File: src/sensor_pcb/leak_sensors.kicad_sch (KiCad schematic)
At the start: 0 parts

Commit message: added connectors
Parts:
- added D1: APHHS1005LSECK/J3-PF, LED_SMD:LED_0402_1005Metric, symbol #dzdb:s_dio/D-KIN-APHHS1005LSECK/J3-PF
- added Q1: NPN BJT 40V 200mA, Package_TO_SOT_SMD:SOT-23, symbol #dzdb:s_misc/Q-NPN-200-SOT23
- added R1, R3: 1k, Resistor_SMD:R_0603_1608Metric, symbol #dzdb:g_res/R-1k-0603
- added R2: 240, Resistor_SMD:R_0603_1608Metric, symbol #dzdb:g_res/R-240-0603
- added R4: 27k, Resistor_SMD:R_0603_1608Metric, symbol #dzdb:g_res/R-27k-0603
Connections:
- new net: D1.2 (A), R2.2
- new net: Q1.1 (B), R3.2, R4.2
- new net GND: D1.1 (K), R1.2
- new net Probe: R3.1
- new net VCC: Q1.2 (E), R4.1
- new net signal: Q1.3 (C), R1.1, R2.1
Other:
- note added: "currently high voltage -> leak detected, could use jumper to change that"
- note added: "will probably want to have multiple ones"

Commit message: 8 pin connectors added
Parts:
- removed D1: APHHS1005LSECK/J3-PF, LED_SMD:LED_0402_1005Metric, symbol #dzdb:s_dio/D-KIN-APHHS1005LSECK/J3-PF
- removed Q1: NPN BJT 40V 200mA, Package_TO_SOT_SMD:SOT-23, symbol #dzdb:s_misc/Q-NPN-200-SOT23
- removed R1, R3: 1k, Resistor_SMD:R_0603_1608Metric, symbol #dzdb:g_res/R-1k-0603
- removed R2: 240, Resistor_SMD:R_0603_1608Metric, symbol #dzdb:g_res/R-240-0603
- removed R4: 27k, Resistor_SMD:R_0603_1608Metric, symbol #dzdb:g_res/R-27k-0603
- added D2, D3: APHHS1005LSECK/J3-PF, LED_SMD:LED_0402_1005Metric, symbol #dzdb:s_dio/D-KIN-APHHS1005LSECK/J3-PF
- added Q2, Q3: NPN BJT 40V 200mA, Package_TO_SOT_SMD:SOT-23, symbol #dzdb:s_misc/Q-NPN-200-SOT23
- added R12, R16: 27k, Resistor_SMD:R_0603_1608Metric, symbol #dzdb:g_res/R-27k-0603
- added R13, R15, R17, R9: 1k, Resistor_SMD:R_0603_1608Metric, symbol #dzdb:g_res/R-1k-0603
- added R14, R18: 240, Resistor_SMD:R_0603_1608Metric, symbol #dzdb:g_res/R-240-0603
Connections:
- net GND: now also D2.1 (K), D3.1 (K), R13.2, R17.2
- net VCC: now also Q2.2 (E), Q3.2 (E), R12.1, R16.1
- new net: Q3.1 (B), R15.2, R16.2
- new net: D2.2 (A), R14.2
- new net: Q2.1 (B), R12.2, R9.2
- new net: D3.2 (A), R18.2
- new net Probe 1.1: R9.1
- new net Probe 2.1: R15.1
- new net sig 1.1: Q2.3 (C), R13.1, R14.1
- new net sig 2.1: Q3.3 (C), R17.1, R18.1
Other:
- note removed: "currently high voltage -> leak detected, could use jumper to change that"
- note removed: "will probably want to have multiple ones"

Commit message: v1 complete
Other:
- company: (none) -> Giacomo Raggi
- title: (none) -> Sensor_pcb: leak sensors
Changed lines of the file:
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@@
 	(generator_version "9.0")
 	(paper "A4")
+	(title_block
+		(title "Sensor_pcb: leak sensors")
+		(date "2025-10-21")
+		(company "Giacomo Raggi")
+	)
 	(rectangle
 		(start 27.94 31.75)

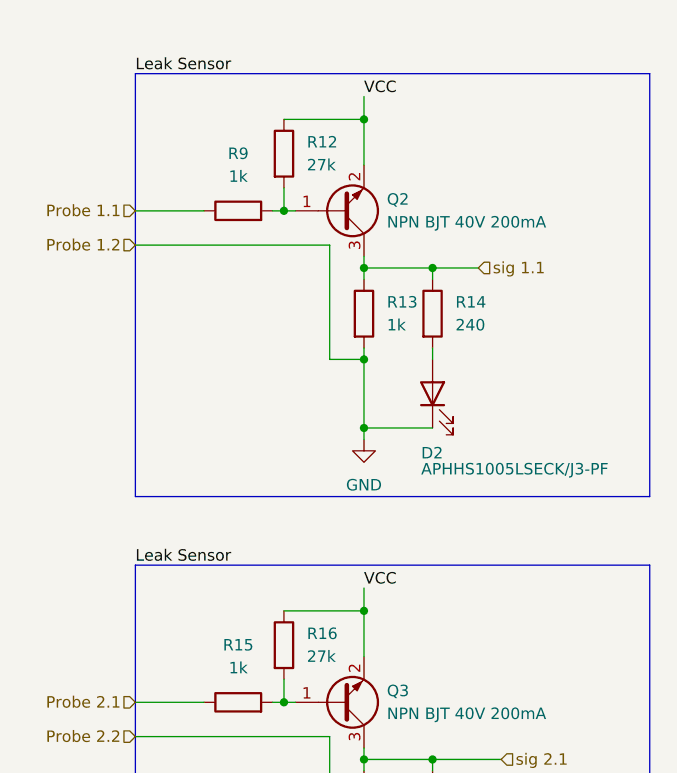
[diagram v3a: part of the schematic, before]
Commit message: schematic update
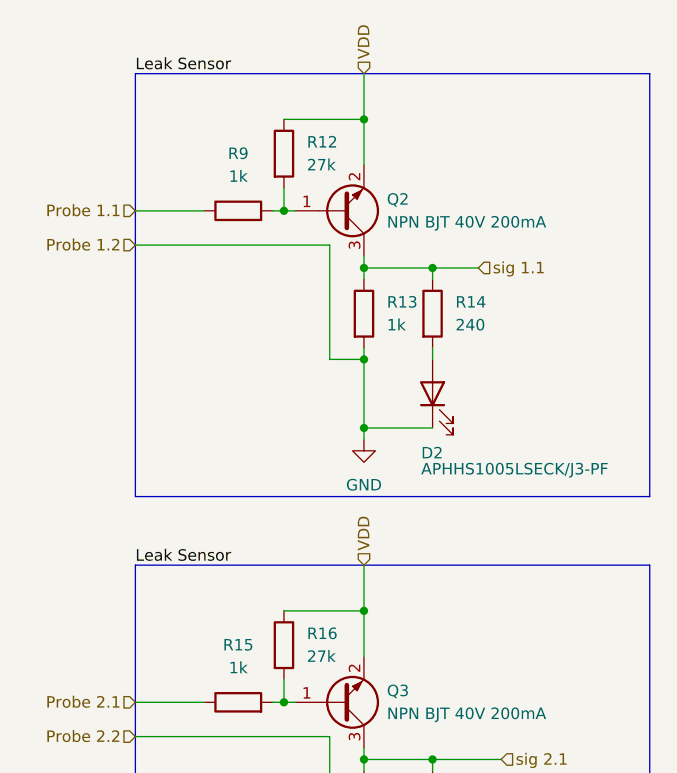
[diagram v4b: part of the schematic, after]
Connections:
- net VCC renamed VDD
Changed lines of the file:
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@@
+	(wire
+		(pts
+			(xy 53.34 31.75) (xy 53.34 36.83)
+		)
+		(stroke
+			(width 0)
+			(type default)
+		)
+	)
+	(wire
+		(pts
+			(xy 53.34 86.36) (xy 53.34 91.44)
+		)
+		(stroke
+			(width 0)
+			(type default)
+		)
+	)
 	(wire
 		(pts
@@
 	(wire
 		(pts
-			(xy 53.34 88.9) (xy 53.34 91.44)
-		)
-		(stroke
-			(width 0)
-			(type default)
-		)
-	)
-	(wire
-		(pts
 			(xy 27.94 101.6) (xy 35.56 101.6)
 		)
@@
 	(wire
 		(pts
-			(xy 53.34 34.29) (xy 53.34 36.83)
-		)
-		(stroke
-			(width 0)
-			(type default)
-		)
-	)
-	(wire
-		(pts
 			(xy 60.96 107.95) (xy 60.96 109.22)
 		)
@@
 			(width 0)
 			(type default)
-		)
-	)
-	(label "VCC"
-		(at 53.34 34.29 0)
-		(effects
-			(font
-				(size 1.27 1.27)
-			)
-			(justify left bottom)
-		)
-	)
-	(label "VCC"
-		(at 53.34 88.9 0)
-		(effects
-			(font
-				(size 1.27 1.27)
-			)
-			(justify left bottom)
 		)
 	)
@@
 		)
 	)
+	(hierarchical_label "VDD"
+		(shape input)
+		(at 53.34 86.36 90)
+		(effects
+			(font
+				(size 1.27 1.27)
+			)
+			(justify left)
+		)
+	)
 	(hierarchical_label "sig 2.1"
 		(shape input)
@@
 		(effects
 			(font
+				(size 1.27 1.27)
+			)
+			(justify left)
+		)
+	)
+	(hierarchical_label "VDD"
+		(shape input)
+		(at 53.34 31.75 90)
+		(effects
+			(font

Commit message: intermediate changes
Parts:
- removed D2, D3: APHHS1005LSECK/J3-PF, LED_SMD:LED_0402_1005Metric, symbol #dzdb:s_dio/D-KIN-APHHS1005LSECK/J3-PF
- added D10, D11, D12, D13, D2, D3: 150060BS73220, dz_dio:LED_0603, symbol #dzdb:s_dio/D-WUR-150060BS73220
- added Q1, Q4, Q5, Q6: NPN BJT 40V 200mA, Package_TO_SOT_SMD:SOT-23, symbol #dzdb:s_misc/Q-NPN-200-SOT23
- added R19, R23, R27, R31: 240, Resistor_SMD:R_0603_1608Metric, symbol #dzdb:g_res/R-240-0603
- added R20, R22, R24, R26, R28, R30, R4, R8: 1k, Resistor_SMD:R_0603_1608Metric, symbol #dzdb:g_res/R-1k-0603
- added R21, R25, R29, R7: 27k, Resistor_SMD:R_0603_1608Metric, symbol #dzdb:g_res/R-27k-0603
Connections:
- net GND: now also D10.C, D11.C, D12.C, D13.C, D2.C, D3.C, R22.2, R26.2, R30.2, R8.2
- net VDD: now also Q1.2 (E), Q4.2 (E), Q5.2 (E), Q6.2 (E), R21.1, R25.1, R29.1, R7.1
- net at R14.2: now also D2.A
- net at R18.2: now also D3.A
- new net: D11.A, R23.2
- new net: Q1.1 (B), R4.2, R7.2
- new net: Q6.1 (B), R28.2, R29.2
- new net: Q5.1 (B), R24.2, R25.2
- new net: D10.A, R19.2
- new net: D12.A, R27.2
- new net: D13.A, R31.2
- new net: Q4.1 (B), R20.2, R21.2
- new net Probe 3.1: R4.1
- new net Probe 4.1: R24.1
- new net Probe 5.1: R20.1
- new net Probe 6.1: R28.1
- new net sig 3.1: Q1.3 (C), R19.1, R8.1
- new net sig 4.1: Q5.3 (C), R26.1, R27.1
- new net sig 5.1: Q4.3 (C), R22.1, R23.1
- new net sig 6.1: Q6.3 (C), R30.1, R31.1
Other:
- moved on the sheet: Q3, R15, R16, R17, R18

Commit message: tuesday changes
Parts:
- added D14, D15: 150060BS73220, dz_dio:LED_0603, symbol #dzdb:s_dio/D-WUR-150060BS73220
- added Q7, Q8: NPN BJT 40V 200mA, Package_TO_SOT_SMD:SOT-23, symbol #dzdb:s_misc/Q-NPN-200-SOT23
- added R32, R34, R36, R38: 1k, Resistor_SMD:R_0603_1608Metric, symbol #dzdb:g_res/R-1k-0603
- added R33, R37: 27k, Resistor_SMD:R_0603_1608Metric, symbol #dzdb:g_res/R-27k-0603
- added R35, R39: 240, Resistor_SMD:R_0603_1608Metric, symbol #dzdb:g_res/R-240-0603
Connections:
- net GND: now also D14.C, D15.C, R34.2, R38.2
- net VDD: now also Q7.2 (E), Q8.2 (E), R33.1, R37.1
- new net: Q7.1 (B), R32.2, R33.2
- new net: D15.A, R39.2
- new net: D14.A, R35.2
- new net: Q8.1 (B), R36.2, R37.2
- new net Probe 7.1: R32.1
- new net Probe 8.1: R36.1
- new net sig 7.1: Q7.3 (C), R34.1, R35.1
- new net sig 8.1: Q8.3 (C), R38.1, R39.1
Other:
- note added: "Leak Sensor"
- moved on the sheet: D10, D11, D12, D13, D2, D3, Q1, Q2, Q3, Q4, Q5, Q6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

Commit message: bom process
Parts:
- removed R14, R18, R19, R23, R27, R31, R35, R39: 240, Resistor_SMD:R_0603_1608Metric, symbol #dzdb:g_res/R-240-0603
- added R14, R19, R43, R44, R45, R46, R47, R48: 1k, Resistor_SMD:R_0603_1608Metric, symbol #dzdb:g_res/R-1k-0603
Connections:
- net sig 1.1: now also R43.1
- net sig 2.1: now also R48.1
- net sig 3.1: now also R14.1
- net sig 4.1: now also R47.1
- net sig 5.1: now also R19.1
- net sig 6.1: now also R46.1
- net sig 7.1: now also R44.1
- net sig 8.1: now also R45.1
- net at D2.A: now also R43.2
- net at D11.A: now also R19.2
- net at D15.A: now also R45.2
- net at D14.A: now also R44.2
- net at D3.A: now also R48.2
- net at D10.A: now also R14.2
- net at D12.A: now also R47.2
- net at D13.A: now also R46.2

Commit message: changes from wrong db
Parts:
- D10, D11, D12, D13, D14, D15, D2, D3: SPN (none) -> 710-150060BS73220
- Q1, Q2, Q3, Q4, Q5, Q6, Q7, Q8: SPN N/A -> 621-MMBT3904-F; Supplier N/A -> Mouser
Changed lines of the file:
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@@
 			)
 		)
-		(property "Supplier" "N/A"
+		(property "Supplier" "Mouser"
 			(at 245.11 34.29 0)
 			(effects
@@
 			)
 		)
-		(property "SPN" "N/A"
+		(property "SPN" "621-MMBT3904-F"
 			(at 245.11 34.29 0)
 			(effects
@@
 			)
 		)
-		(property "SPN" ""
+		(property "SPN" "710-150060BS73220"
 			(at 57.15 58.42 0)
 			(effects
@@
 			)
 		)
-		(property "Supplier" "N/A"
+		(property "Supplier" "Mouser"
 			(at 177.8 93.98 0)
 			(effects
@@
 			)
 		)
-		(property "SPN" "N/A"
+		(property "SPN" "621-MMBT3904-F"
 			(at 177.8 93.98 0)
 			(effects
@@
 			)
 		)
-		(property "Supplier" "N/A"
+		(property "Supplier" "Mouser"
 			(at 113.03 93.98 0)
 			(effects
@@
 			)
 		)
-		(property "SPN" "N/A"
+		(property "SPN" "621-MMBT3904-F"
 			(at 113.03 93.98 0)
 			(effects
@@
 			)
 		)
-		(property "Supplier" "N/A"
+		(property "Supplier" "Mouser"
 			(at 48.26 93.98 0)
 			(effects
@@
 			)
 		)
-		(property "SPN" "N/A"
+		(property "SPN" "621-MMBT3904-F"
 			(at 48.26 93.98 0)
 			(effects
@@
 			)
 		)
-		(property "SPN" ""
+		(property "SPN" "710-150060BS73220"
 			(at 254 118.11 0)
 			(effects
@@
 			)
 		)
-		(property "Supplier" "N/A"
+		(property "Supplier" "Mouser"
 			(at 114.3 34.29 0)
 			(effects
@@
 			)
 		)
-		(property "SPN" "N/A"
+		(property "SPN" "621-MMBT3904-F"
 			(at 114.3 34.29 0)
 			(effects
@@
 			)
 		)
-		(property "SPN" ""
+		(property "SPN" "710-150060BS73220"
 			(at 124.46 58.42 0)
 			(effects
@@
 			)
 		)
-		(property "Supplier" "N/A"
+		(property "Supplier" "Mouser"
 			(at 243.84 93.98 0)
 			(effects
@@
 			)
 		)
-		(property "SPN" "N/A"
+		(property "SPN" "621-MMBT3904-F"
 			(at 243.84 93.98 0)
 			(effects
@@
 			)
 		)
-		(property "SPN" ""
+		(property "SPN" "710-150060BS73220"
 			(at 58.42 118.11 0)
 			(effects
@@
 			)
 		)
-		(property "SPN" ""
+		(property "SPN" "710-150060BS73220"
 			(at 187.96 118.11 0)
 			(effects
@@
 			)
 		)
-		(property "Supplier" "N/A"
+		(property "Supplier" "Mouser"
 			(at 46.99 34.29 0)
 			(effects
@@
 			)
 		)
-		(property "SPN" "N/A"
+		(property "SPN" "621-MMBT3904-F"
 			(at 46.99 34.29 0)
 			(effects
@@
 			)
 		)
-		(property "Supplier" "N/A"
+		(property "Supplier" "Mouser"
 			(at 179.07 34.29 0)
 			(effects
@@
 			)
 		)
-		(property "SPN" "N/A"
+		(property "SPN" "621-MMBT3904-F"
 			(at 179.07 34.29 0)
 			(effects
@@
 			)
 		)
-		(property "SPN" ""
+		(property "SPN" "710-150060BS73220"
 			(at 123.19 118.11 0)
 			(effects
@@
 			)
 		)
-		(property "SPN" ""
+		(property "SPN" "710-150060BS73220"
 			(at 189.23 58.42 0)
 			(effects
@@
 			)
 		)
-		(property "SPN" ""
+		(property "SPN" "710-150060BS73220"
 			(at 255.27 58.42 0)
 			(effects
